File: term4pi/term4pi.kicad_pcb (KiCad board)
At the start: 2 copper layers, 3 x 56.5 mm, 22 parts, among them J1 USB_B_Micro, J2 PiHeader, J3 PWR, J4 UART, U1 CP2102N-A01-GQFN24

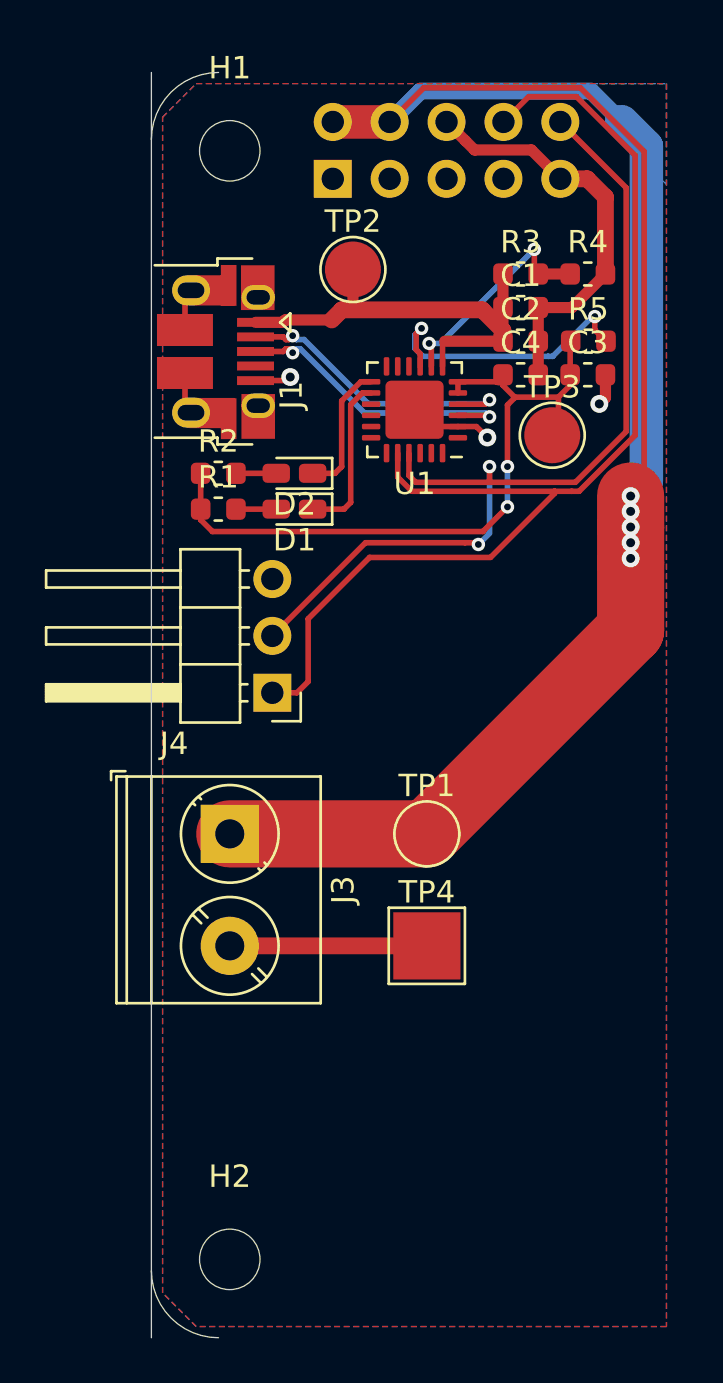
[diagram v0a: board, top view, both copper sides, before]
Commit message: Fix edge cuts.
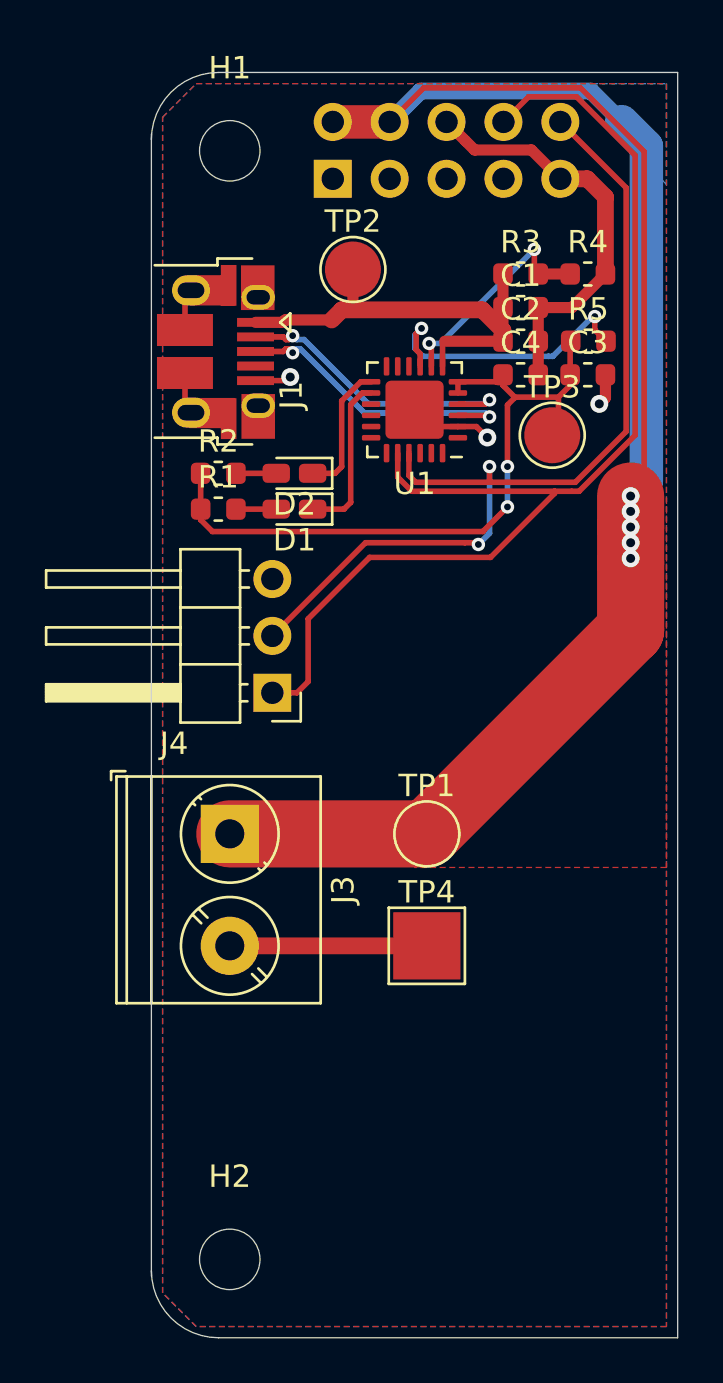
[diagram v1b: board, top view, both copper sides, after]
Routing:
- added copper zone on F.Cu, net +5V
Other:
- board size 3 x 56.5 mm -> 23.5 x 56.5 mm
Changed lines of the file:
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@@
   (general
     (thickness 1.6)
-    (drawings 3)
+    (drawings 6)
     (tracks 189)
     (zones 0)
@@
     )
   )
+  (gr_line (start 123.5 131.5) (end 103 131.5) (layer Edge.Cuts) (width 0.05))
+  (gr_line (start 123.5 75) (end 123.5 131.5) (layer Edge.Cuts) (width 0.05))
+  (gr_line (start 103 75) (end 123.5 75) (layer Edge.Cuts) (width 0.05))
   (gr_arc (start 103 128.5) (end 100 128.5) (angle -90) (layer Edge.Cuts) (width 0.05))
   (gr_arc (start 103 78) (end 103 75) (angle -90) (layer Edge.Cuts) (width 0.05))
-  (gr_line (start 100 75) (end 100 131.5) (layer Edge.Cuts) (width 0.05))
+  (gr_line (start 100 77.75) (end 100 128.75) (layer Edge.Cuts) (width 0.05))
   (segment (start 105.970249 86.052599) (end 108.052599 86.052599) (width 0.5) (layer F.Cu) (net 1))
   (segment (start 105.862848 86.16) (end 105.970249 86.052599) (width 0.5) (layer F.Cu) (net 1))
@@
       )
     )
+  )
+  (zone (net 12) (net_name +5V) (layer F.Cu) (hatch edge 0.508)
+    (priority 1)
+    (connect_pads (clearance 0.508))
+    (min_thickness 0.254)
+    (fill yes (arc_segments 32) (thermal_gap 0.254) (thermal_bridge_width 0.508))
+    (polygon
+      (pts
+        (xy 123 110.5) (xy 111.75 110.5) (xy 111.75 107.5) (xy 120 99.25) (xy 120 94)
+        (xy 123 94)
+      )
+    )

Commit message: Update term4pi
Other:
- outline, holes or cut-outs redrawn
- board text added: "+"
- board text added: "+5V"
- board text added: "-"
- board text added: "GND"
- board text added: "PI RX"
- board text added: "PI TX"
- board text added: "Term4Pi"
- board text added: "VBUS"
- board text added: "VDD"
- board text added: "v1 (C) 2020 Matir"
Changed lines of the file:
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@@
   (general
     (thickness 1.6)
-    (drawings 6)
+    (drawings 17)
     (tracks 189)
     (zones 0)
@@
     (trace_clearance 0.1524)
     (zone_clearance 0.508)
-    (zone_45_only no)
+    (zone_45_only yes)
     (trace_min 0.2)
     (via_size 0.8)
@@
       (outputformat 1)
       (mirror false)
-      (drillshape 1)
+      (drillshape 0)
       (scaleselection 1)
-      (outputdirectory ""))
+      (outputdirectory "output/"))
   )
   (net 0 "")
@@
     (tags capacitor)
     (attr smd)
-    (fp_text reference C1 (at 0 -1.43) (layer F.SilkS)
-      (effects (font (size 1 1) (thickness 0.15)))
+    (fp_text reference C1 (at -3.75 -2) (layer F.SilkS)
+      (effects (font (size 0.6 0.6) (thickness 0.15)))
     )
     (fp_text value 4.7uF (at 0 1.43) (layer F.Fab)
@@
     (tags capacitor)
     (attr smd)
-    (fp_text reference C2 (at 0 -1.43) (layer F.SilkS)
-      (effects (font (size 1 1) (thickness 0.15)))
+    (fp_text reference C2 (at -3.75 -2.5) (layer F.SilkS)
+      (effects (font (size 0.6 0.6) (thickness 0.15)))
     )
     (fp_text value 0.1uF (at 0 1.43) (layer F.Fab)
@@
     (tags capacitor)
     (attr smd)
-    (fp_text reference C3 (at 0 -1.43) (layer F.SilkS)
-      (effects (font (size 1 1) (thickness 0.15)))
+    (fp_text reference C3 (at -5.2375 -3) (layer F.SilkS)
+      (effects (font (size 0.6 0.6) (thickness 0.15)))
     )
     (fp_text value 4.7uF (at 0 1.43) (layer F.Fab)
@@
     (tags capacitor)
     (attr smd)
-    (fp_text reference C4 (at 0 -1.43) (layer F.SilkS)
-      (effects (font (size 1 1) (thickness 0.15)))
+    (fp_text reference C4 (at -3.75 -3) (layer F.SilkS)
+      (effects (font (size 0.6 0.6) (thickness 0.15)))
     )
     (fp_text value 0.1uF (at 0 1.43) (layer F.Fab)
@@
     (tags "LED castellated")
     (attr smd)
-    (fp_text reference D1 (at 0 -1.38) (layer F.SilkS)
-      (effects (font (size 1 1) (thickness 0.15)))
+    (fp_text reference D1 (at -4.1125 -0.25) (layer F.SilkS)
+      (effects (font (size 0.6 0.6) (thickness 0.15)))
     )
     (fp_text value LED (at 0 1.38) (layer F.Fab)
@@
     (tags "LED castellated")
     (attr smd)
-    (fp_text reference D2 (at 0 -1.38) (layer F.SilkS)
-      (effects (font (size 1 1) (thickness 0.15)))
+    (fp_text reference D2 (at -4.1125 -0.85) (layer F.SilkS)
+      (effects (font (size 0.6 0.6) (thickness 0.15)))
     )
     (fp_text value LED (at 0 1.38) (layer F.Fab)
@@
     (tags "mounting hole 2.7mm no annular m2.5")
     (attr virtual)
-    (fp_text reference H1 (at 0 -3.7) (layer F.SilkS)
+    (fp_text reference H1 (at 0 -3.7) (layer F.SilkS) hide
       (effects (font (size 1 1) (thickness 0.15)))
     )
@@
     (tags "mounting hole 2.7mm no annular m2.5")
     (attr virtual)
-    (fp_text reference H2 (at 0 -3.7) (layer F.SilkS)
+    (fp_text reference H2 (at 0 -3.7) (layer F.SilkS) hide
       (effects (font (size 1 1) (thickness 0.15)))
     )
@@
     (tags "USB USB_B USB_micro USB_OTG")
     (attr smd)
-    (fp_text reference J1 (at 1.925 -3.365 90) (layer F.SilkS)
-      (effects (font (size 1 1) (thickness 0.15)))
+    (fp_text reference J1 (at -4.735 1.635 180) (layer F.SilkS)
+      (effects (font (size 0.6 0.6) (thickness 0.15)))
     )
     (fp_text value USB_B_Micro (at -0.025 4.435 90) (layer F.Fab)
@@
     (descr "Terminal Block Phoenix PT-1,5-2-5.0-H, 2 pins, pitch 5mm, size 10x9mm^2, drill diamater 1.3mm, pad diameter 2.6mm, see http://www.mouser.com/ds/2/324/ItemDetail_1935161-922578.pdf, script-generated using https://github.com/pointhi/kicad-footprint-generator/scripts/TerminalBlock_Phoenix")
     (tags "THT Terminal Block Phoenix PT-1,5-2-5.0-H pitch 5mm size 10x9mm^2 drill 1.3mm pad 2.6mm")
-    (fp_text reference J3 (at 2.5 -5.06 90) (layer F.SilkS)
-      (effects (font (size 1 1) (thickness 0.15)))
+    (fp_text reference J3 (at 8.5 -1.5 180) (layer F.SilkS)
+      (effects (font (size 0.6 0.6) (thickness 0.15)))
     )
     (fp_text value PWR (at 2.5 6.06 90) (layer F.Fab)
@@
     (descr "Through hole angled pin header, 1x03, 2.54mm pitch, 6mm pin length, single row")
     (tags "Through hole angled pin header THT 1x03 2.54mm single row")
-    (fp_text reference J4 (at 4.385 -2.27) (layer F.SilkS)
-      (effects (font (size 1 1) (thickness 0.15)))
+    (fp_text reference J4 (at 1.4 -2.3) (layer F.SilkS)
+      (effects (font (size 0.6 0.6) (thickness 0.15)))
     )
     (fp_text value UART (at 4.385 7.35) (layer F.Fab)
@@
     (tags resistor)
     (attr smd)
-    (fp_text reference R1 (at 0 -1.43) (layer F.SilkS)
-      (effects (font (size 1 1) (thickness 0.15)))
+    (fp_text reference R1 (at 6.0125 0.25) (layer F.SilkS)
+      (effects (font (size 0.6 0.6) (thickness 0.15)))
     )
     (fp_text value 1k (at 0 1.43) (layer F.Fab)
@@
     (tags resistor)
     (attr smd)
-    (fp_text reference R2 (at 0 -1.43) (layer F.SilkS)
-      (effects (font (size 1 1) (thickness 0.15)))
+    (fp_text reference R2 (at 6.0125 0.85) (layer F.SilkS)
+      (effects (font (size 0.6 0.6) (thickness 0.15)))
     )
     (fp_text value 1k (at 0 1.43) (layer F.Fab)
@@
     (tags resistor)
     (attr smd)
-    (fp_text reference R3 (at 0 -1.43) (layer F.SilkS)
-      (effects (font (size 1 1) (thickness 0.15)))
+    (fp_text reference R3 (at -3.75 -1.43) (layer F.SilkS)
+      (effects (font (size 0.6 0.6) (thickness 0.15)))
     )
     (fp_text value 22.1k (at 0 1.43) (layer F.Fab)
@@
     (tags resistor)
     (attr smd)
-    (fp_text reference R4 (at 0 -1.43) (layer F.SilkS)
-      (effects (font (size 1 1) (thickness 0.15)))
+    (fp_text reference R4 (at -5.2375 -1.43) (layer F.SilkS)
+      (effects (font (size 0.6 0.6) (thickness 0.15)))
     )
     (fp_text value 47.5k (at 0 1.43) (layer F.Fab)
@@
     (tags resistor)
     (attr smd)
-    (fp_text reference R5 (at 0 -1.43) (layer F.SilkS)
-      (effects (font (size 1 1) (thickness 0.15)))
+    (fp_text reference R5 (at -5.2625 -2.5) (layer F.SilkS)
+      (effects (font (size 0.6 0.6) (thickness 0.15)))
     )
     (fp_text value 1k (at 0 1.43) (layer F.Fab)
@@
     (tags "test point SMD pad")
     (attr virtual)
-    (fp_text reference TP1 (at 0 -2.148) (layer F.SilkS)
+    (fp_text reference TP1 (at 0 -2.148) (layer F.SilkS) hide
       (effects (font (size 1 1) (thickness 0.15)))
     )
@@
     (tags "test point SMD pad")
     (attr virtual)
-    (fp_text reference TP2 (at 0 -2.148) (layer F.SilkS)
+    (fp_text reference TP2 (at 0 -2.148) (layer F.SilkS) hide
       (effects (font (size 1 1) (thickness 0.15)))
     )
@@
     (tags "test point SMD pad")
     (attr virtual)
-    (fp_text reference TP3 (at 0 -2.148) (layer F.SilkS)
+    (fp_text reference TP3 (at 0 -2.148) (layer F.SilkS) hide
       (effects (font (size 1 1) (thickness 0.15)))
     )
@@
     (tags "test point SMD pad rectangle square")
     (attr virtual)
-    (fp_text reference TP4 (at 0 -2.398) (layer F.SilkS)
+    (fp_text reference TP4 (at 0 -2.398) (layer F.SilkS) hide
       (effects (font (size 1 1) (thickness 0.15)))
     )
@@
     (tags "QFN DFN_QFN")
     (attr smd)
-    (fp_text reference U1 (at 0 -3.3) (layer F.SilkS)
+    (fp_text reference U1 (at -2 -3.1875) (layer F.SilkS)
       (effects (font (size 1 1) (thickness 0.15)))
     )
@@
     )
   )
+  (gr_text "v1\n(C) 2020 Matir" (at 108.75 129.25) (layer F.SilkS)
+    (effects (font (size 0.75 0.75) (thickness 0.15)) (justify left))
+  )
+  (gr_text Term4Pi (at 108.5 126.75) (layer F.SilkS)
+    (effects (font (size 1 1) (thickness 0.15)) (justify left))
+  )
+  (gr_text "PI TX" (at 109.25 102.75) (layer F.SilkS)
+    (effects (font (size 1 1) (thickness 0.15)))
+  )
+  (gr_text "PI RX" (at 109.25 100.25) (layer F.SilkS)
+    (effects (font (size 1 1) (thickness 0.15)))
+  )
+  (gr_text GND (at 108.75 97.75) (layer F.SilkS)
+    (effects (font (size 1 1) (thickness 0.15)))
+  )
+  (gr_text - (at 109.25 114) (layer F.SilkS)
+    (effects (font (size 2 2) (thickness 0.3)))
+  )
+  (gr_text + (at 109.25 109) (layer F.SilkS)
+    (effects (font (size 2 2) (thickness 0.3)))
+  )
+  (gr_text GND (at 115.75 115) (layer F.SilkS)
+    (effects (font (size 1 1) (thickness 0.15)))
+  )
+  (gr_text +5V (at 115.5 110) (layer F.SilkS)
+    (effects (font (size 1 1) (thickness 0.15)))
+  )
+  (gr_text VDD (at 117.75 93.5) (layer F.SilkS)
+    (effects (font (size 1 1) (thickness 0.15)))
+  )
+  (gr_text VBUS (at 109 86) (layer F.SilkS)
+    (effects (font (size 1 1) (thickness 0.15)))
+  )
   (gr_line (start 123.5 131.5) (end 103 131.5) (layer Edge.Cuts) (width 0.05))
   (gr_line (start 123.5 75) (end 123.5 131.5) (layer Edge.Cuts) (width 0.05))
@@
   (gr_arc (start 103 128.5) (end 100 128.5) (angle -90) (layer Edge.Cuts) (width 0.05))
   (gr_arc (start 103 78) (end 103 75) (angle -90) (layer Edge.Cuts) (width 0.05))
-  (gr_line (start 100 77.75) (end 100 128.75) (layer Edge.Cuts) (width 0.05))
+  (gr_line (start 100 78) (end 100 128.5) (layer Edge.Cuts) (width 0.05))
   (segment (start 105.970249 86.052599) (end 108.052599 86.052599) (width 0.5) (layer F.Cu) (net 1))
   (segment (start 105.862848 86.16) (end 105.970249 86.052599) (width 0.5) (layer F.Cu) (net 1))
@@
       )
     )
+  )
+  (zone (net 12) (net_name +5V) (layer F.Cu) (hatch edge 0.508)
+    (priority 1)
+    (connect_pads (clearance 0.508))
+    (min_thickness 0.254)
+    (fill yes (arc_segments 32) (thermal_gap 0.254) (thermal_bridge_width 0.508))
+    (polygon
+      (pts
+        (xy 111.75 78.25) (xy 106.25 78.25) (xy 106.25 75.5) (xy 111.75 75.5)
+      )
+    )
+  )
+  (zone (net 12) (net_name +5V) (layer B.Cu) (hatch edge 0.508)
+    (priority 1)
+    (connect_pads (clearance 0.508))
+    (min_thickness 0.254)
+    (fill yes (arc_segments 32) (thermal_gap 0.254) (thermal_bridge_width 0.508))
+    (polygon
+      (pts
+        (xy 111.75 78.25) (xy 106.25 78.25) (xy 106.25 75.5) (xy 111.75 75.5)
+      )
+    )
